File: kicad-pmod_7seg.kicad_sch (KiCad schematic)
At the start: 33 parts, among them Q1 MMBT3906, Q2 MMBT3906, Q3 MMBT3906, Q4 MMBT3906, U1 7447, U2 7442, U3 CA56-12CGKWA

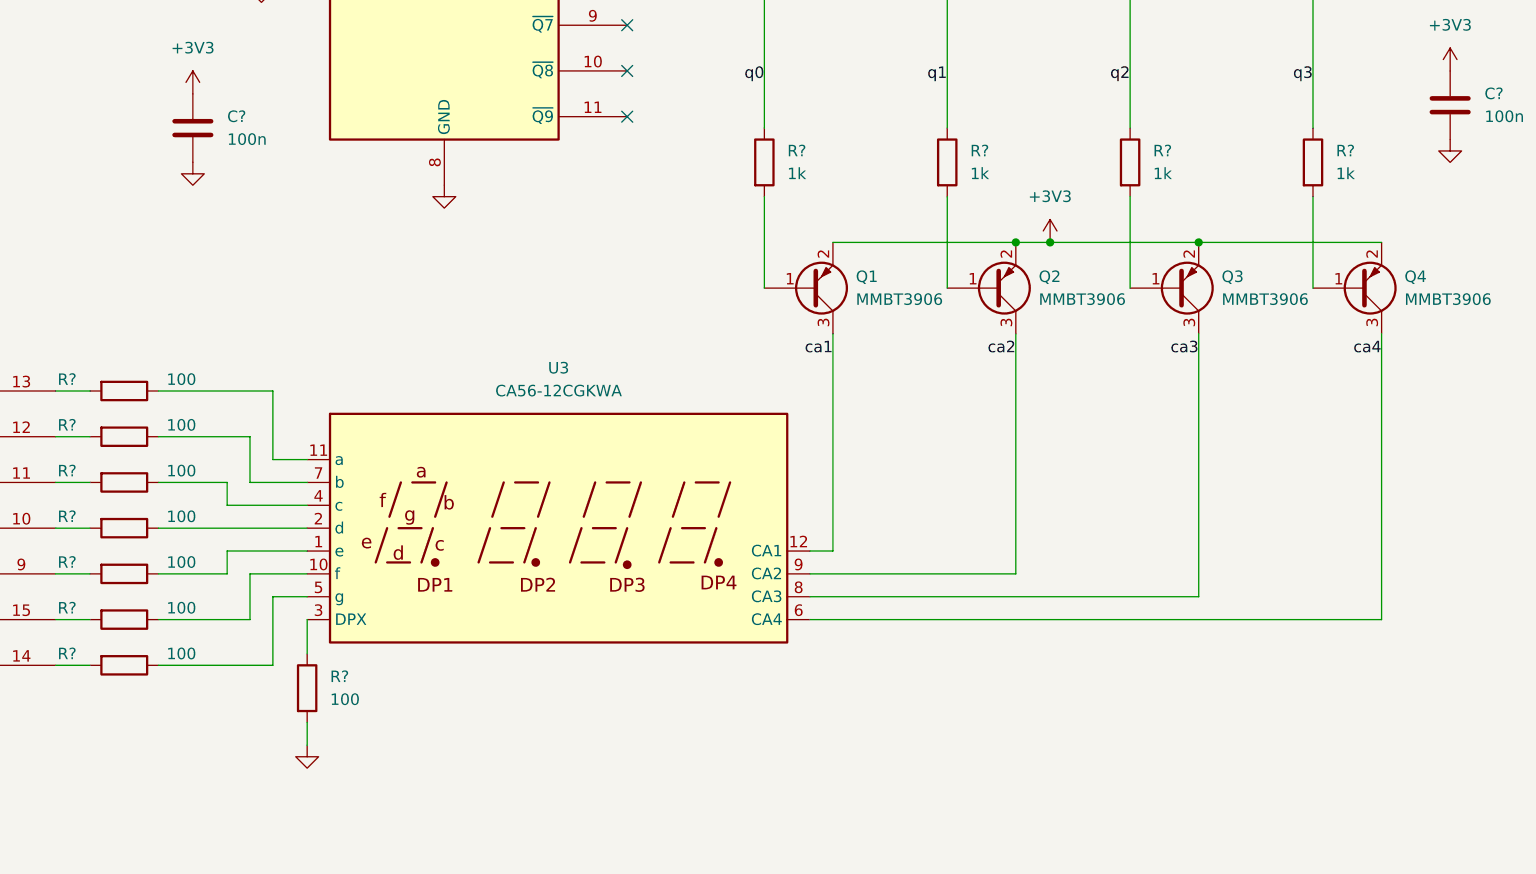
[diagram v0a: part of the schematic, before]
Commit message: updated resistoor values
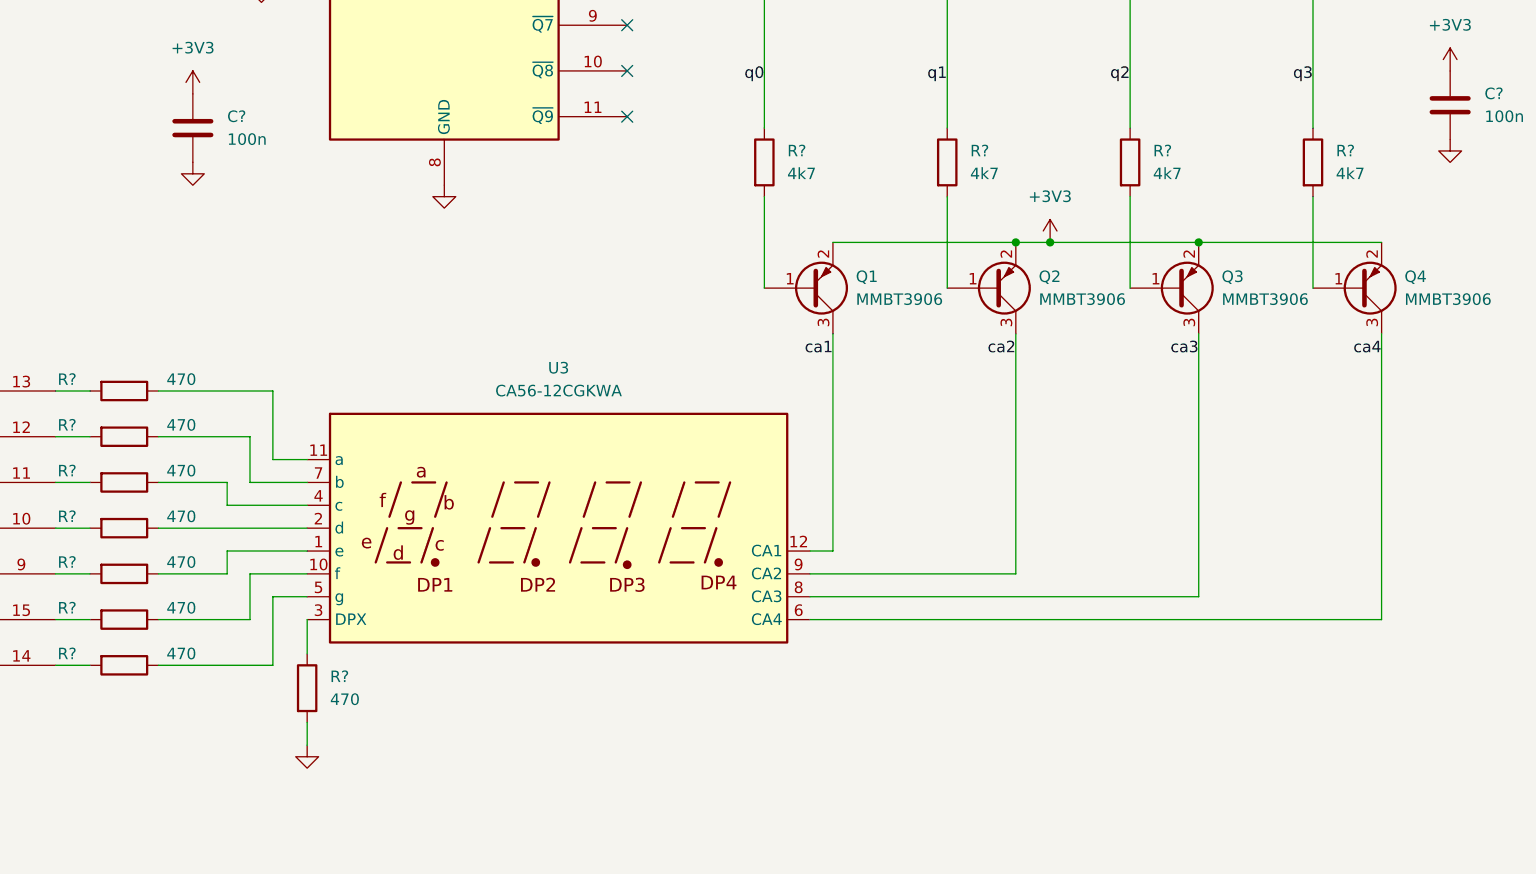
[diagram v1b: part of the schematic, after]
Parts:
- R? (x8): value 100 -> 470
- R? (x4): value 1k -> 4k7
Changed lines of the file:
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@@
       (effects (font (size 1.27 1.27)))
     )
-    (property "Value" "100" (at 129.54 135.89 90)
+    (property "Value" "470" (at 129.54 135.89 90)
       (effects (font (size 1.27 1.27)))
     )
@@
       (effects (font (size 1.27 1.27)))
     )
-    (property "Value" "100" (at 129.54 140.97 90)
+    (property "Value" "470" (at 129.54 140.97 90)
       (effects (font (size 1.27 1.27)))
     )
@@
       (effects (font (size 1.27 1.27)))
     )
-    (property "Value" "100" (at 129.54 110.49 90)
+    (property "Value" "470" (at 129.54 110.49 90)
       (effects (font (size 1.27 1.27)))
     )
@@
       (effects (font (size 1.27 1.27)))
     )
-    (property "Value" "100" (at 129.54 130.81 90)
+    (property "Value" "470" (at 129.54 130.81 90)
       (effects (font (size 1.27 1.27)))
     )
@@
       (effects (font (size 1.27 1.27)) (justify left))
     )
-    (property "Value" "1k" (at 196.85 87.63 0)
+    (property "Value" "4k7" (at 196.85 87.63 0)
       (effects (font (size 1.27 1.27)) (justify left))
     )
@@
       (effects (font (size 1.27 1.27)))
     )
-    (property "Value" "100" (at 129.54 115.57 90)
+    (property "Value" "470" (at 129.54 115.57 90)
       (effects (font (size 1.27 1.27)))
     )
@@
       (effects (font (size 1.27 1.27)) (justify left))
     )
-    (property "Value" "1k" (at 237.49 87.63 0)
+    (property "Value" "4k7" (at 237.49 87.63 0)
       (effects (font (size 1.27 1.27)) (justify left))
     )
@@
       (effects (font (size 1.27 1.27)) (justify left))
     )
-    (property "Value" "1k" (at 257.81 87.63 0)
+    (property "Value" "4k7" (at 257.81 87.63 0)
       (effects (font (size 1.27 1.27)) (justify left))
     )
@@
       (effects (font (size 1.27 1.27)) (justify left))
     )
-    (property "Value" "1k" (at 217.17 87.63 0)
+    (property "Value" "4k7" (at 217.17 87.63 0)
       (effects (font (size 1.27 1.27)) (justify left))
     )
@@
       (effects (font (size 1.27 1.27)))
     )
-    (property "Value" "100" (at 129.54 125.73 90)
+    (property "Value" "470" (at 129.54 125.73 90)
       (effects (font (size 1.27 1.27)))
     )
@@
       (effects (font (size 1.27 1.27)) (justify left))
     )
-    (property "Value" "100" (at 146.05 146.05 0)
+    (property "Value" "470" (at 146.05 146.05 0)
       (effects (font (size 1.27 1.27)) (justify left))
     )
@@
       (effects (font (size 1.27 1.27)))
     )
-    (property "Value" "100" (at 129.54 120.65 90)
-      (effects (font (size 1.27 1.27)))
-    )
+    (property "Value" "470" (at 129.54 120.65 90)
+      (effects (font (size 1.27 1.27)))
+    )
